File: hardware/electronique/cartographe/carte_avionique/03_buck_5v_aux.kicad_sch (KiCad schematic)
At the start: 10 parts, among them J301 SORTIE 5V_AUX, U301 LM76003 / 5V_AUX

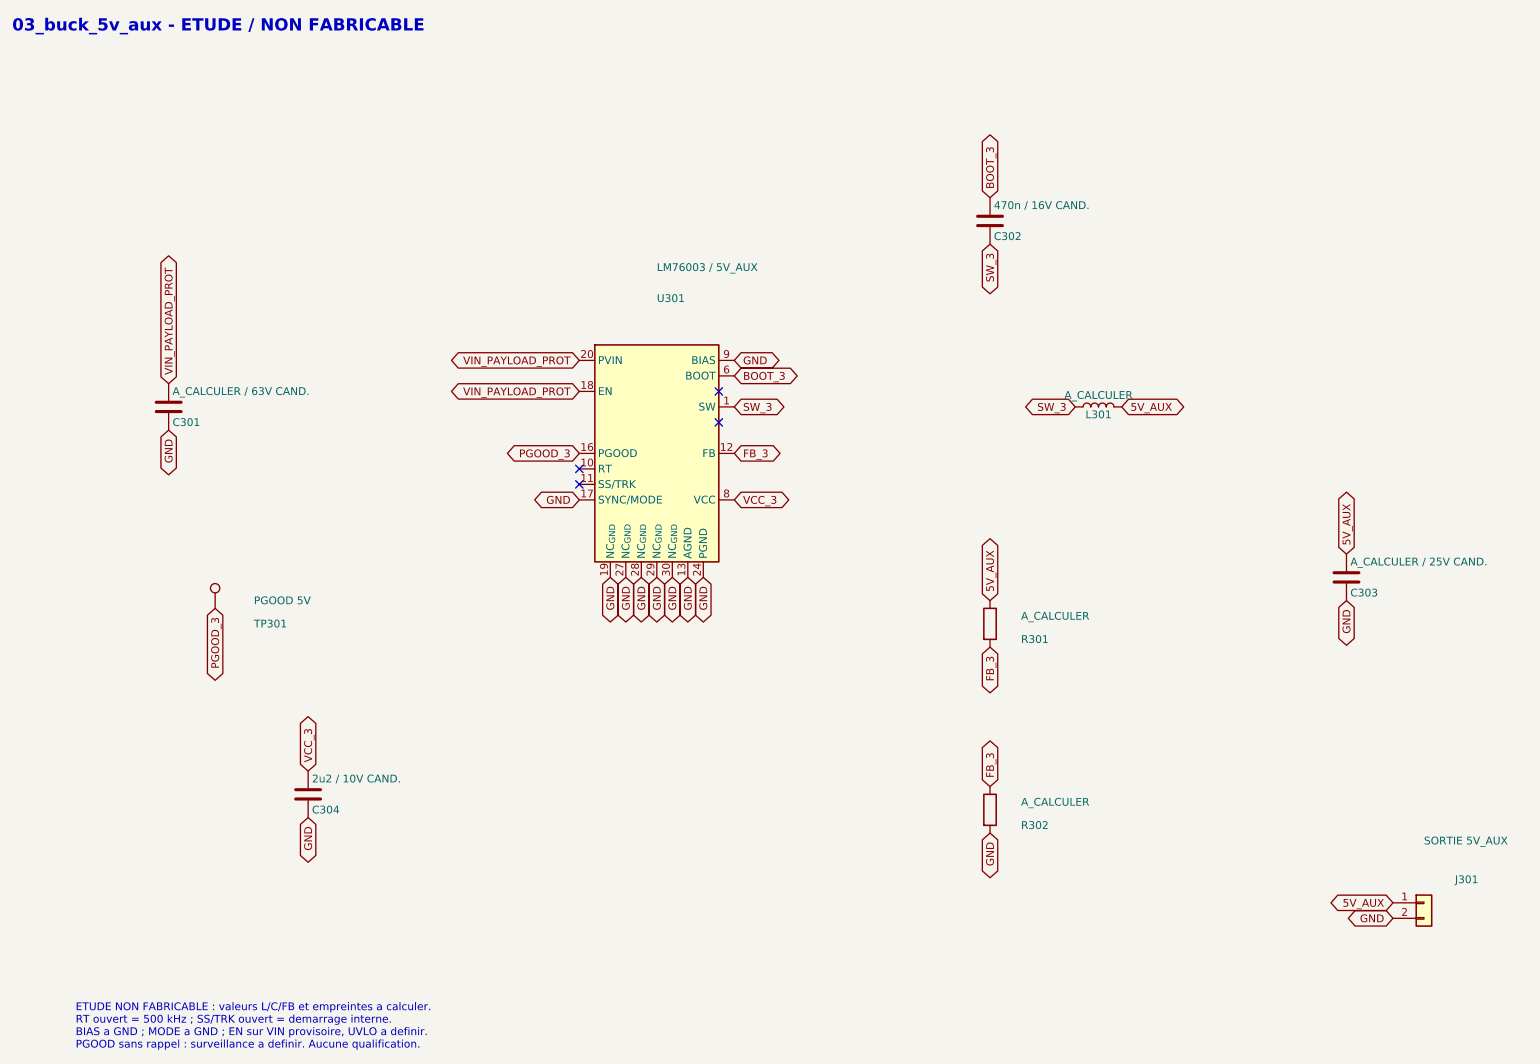
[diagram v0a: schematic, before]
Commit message: feat(hw): compléter CA01 et clarifier la synchronisation des captures
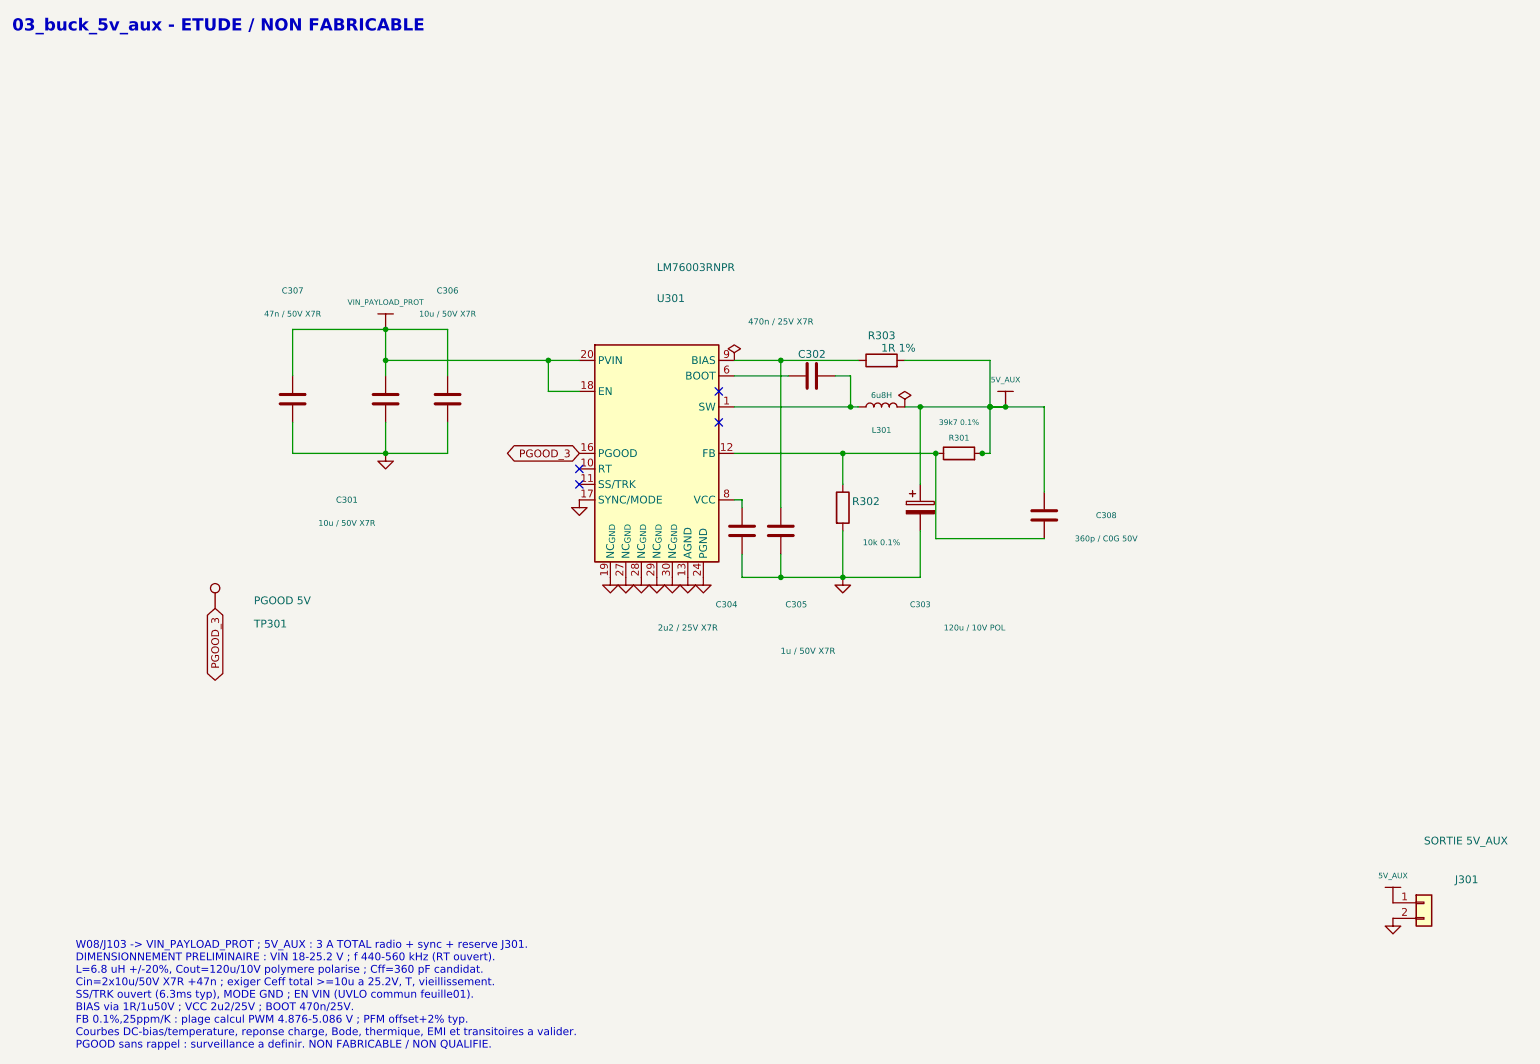
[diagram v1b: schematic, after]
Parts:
- added C305: 1u / 50V X7R, Capacitor_SMD:C_0603_1608Metric, symbol Device:C
- added C306: 10u / 50V X7R, Capacitor_SMD:C_1210_3225Metric, symbol Device:C
- added C307: 47n / 50V X7R, Capacitor_SMD:C_0603_1608Metric, symbol Device:C
- added C308: 360p / C0G 50V, Capacitor_SMD:C_0603_1608Metric, symbol Device:C
- added R303: 1R 1%, Resistor_SMD:R_0603_1608Metric, symbol Device:R
- C301: value A_CALCULER / 63V CAND. -> 10u / 50V X7R; footprint (none) -> Capacitor_SMD:C_1210_3225Metric; Design_status (none) -> A valider - calcul preliminaire 2026-09-29; MPN (none) -> C3225X7R1H106K250AC; Manufacturer (none) -> TDK
- C302: value 470n / 16V CAND. -> 470n / 25V X7R; footprint (none) -> Capacitor_SMD:C_0603_1608Metric; Design_status (none) -> A valider - calcul preliminaire 2026-09-29; MPN (none) -> C1608X7R1E474K080AB; Manufacturer (none) -> TDK
- C303: value A_CALCULER / 25V CAND. -> 120u / 10V POL; footprint (none) -> Capacitor_SMD:CP_Elec_6.3x5.9; symbol Device:C -> Device:C_Polarized; Design_status (none) -> A valider - calcul preliminaire 2026-09-29; MPN (none) -> 10SVPC120MV; Manufacturer (none) -> Panasonic
- C304: value 2u2 / 10V CAND. -> 2u2 / 25V X7R; footprint (none) -> Capacitor_SMD:C_0805_2012Metric; Design_status (none) -> A valider - calcul preliminaire 2026-09-29; MPN (none) -> C2012X7R1E225K125AB; Manufacturer (none) -> TDK
- L301: value A_CALCULER -> 6u8H; footprint (none) -> Inductor_SMD:L_Coilcraft_XAL1010-XXX; Design_status (none) -> A valider - calcul preliminaire 2026-09-29; MPN (none) -> XAL1010-682MED; Manufacturer (none) -> Coilcraft
- R301: value A_CALCULER -> 39k7 0.1%; footprint (none) -> Resistor_SMD:R_0603_1608Metric; Design_status (none) -> A valider - calcul preliminaire 2026-09-29; MPN (none) -> TNPW060339K7BEEA; Manufacturer (none) -> Vishay
- R302: value A_CALCULER -> 10k 0.1%; footprint (none) -> Resistor_SMD:R_0603_1608Metric; Design_status (none) -> A valider - calcul preliminaire 2026-09-29; MPN (none) -> TNPW060310K0BEEA; Manufacturer (none) -> Vishay
- U301: value LM76003 / 5V_AUX -> LM76003RNPR; Design_status (none) -> A valider - calcul preliminaire 2026-09-29; MPN (none) -> LM76003RNPR; Manufacturer (none) -> Texas Instruments
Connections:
- net 5V_AUX: now also R301.2, C308.1, R303.2; no longer R301.1
- net GND: now also C305.2, C306.2, C307.2; no longer U301.9 (BIAS)
- net VIN_PAYLOAD_PROT: now also C306.1, C307.1
- net BOOT_3: no longer names the net of C302.1, U301.6 (BOOT)
- net FB_3: no longer names the net of R302.1, U301.12 (FB)
- net FB_3: now also R301.1, C308.2; no longer R301.2
- net SW_3: no longer names the net of C302.2, L301.1, U301.1 (SW), U301.2 (SW), U301.3 (SW), U301.4 (SW), U301.5 (SW)
- net VCC_3: no longer names the net of C304.1, U301.8 (VCC)
- new net: C305.1, R303.1, U301.9 (BIAS)
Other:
- note added: "W08/J103 -> VIN_PAYLOAD_PROT ; 5V_AUX : 3 A TOTAL radio + sync + reserve J301. DIMENSIONNEMENT PRELIMINAIRE : VIN 18-25.2 V ; f 440-560 kHz (RT ouvert). L=6.8 uH +/-20%, Cout=120u/10V polymere polarise ; Cff=360 pF candidat. Cin=2x10u/50V X7R +47n ; exiger Ceff total >=10u a 25.2V, T, vieillissement. SS/TRK ouvert (6.3ms typ), MODE GND ; EN VIN (UVLO commun feuille01). BIAS via 1R/1u50V ; VCC 2u2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"
- note removed: "ETUDE NON FABRICABLE : valeurs L/C/FB et empreintes a calculer. RT ouvert = 500 kHz ; SS/TRK ouvert = demarrage interne. BIAS a GND ; MODE a GND ; EN sur VIN provisoire, UVLO a definir. PGOOD sans rappel : surveillance a definir. Aucune qualification."
- moved on the sheet: C301, C302, C304, L301, R301, R302
